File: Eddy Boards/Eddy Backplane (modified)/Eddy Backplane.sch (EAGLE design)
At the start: 88 parts, among them J1 USB_MINI-B_SMT, P1 39-30-02_S, P2 RB1-125BAG1A, P3 39-30-04_S, Q1 310mA/60V/1.6Ω, Q2 310mA/60V/1.6Ω, Q3 310mA/60V/1.6Ω, Q4 310mA/60V/1.6Ω, Q5 310mA/60V/1.6Ω, Q6 310mA/60V/1.6Ω, Q7 310mA/60V/1.6Ω, Q8 310mA/60V/1.6Ω, U1 W5500, U2 STM32F405RGT6, Y2 12MHz, Y3 32.768kHz

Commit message: Routing began on Eddy backplane. New size
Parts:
- removed 16MHZ, 32.768KHZ: (no value), SparkFun-Clocks:CRYSTALPTH-HC49US
- removed C10, C11, C12, C9: (no value), rcl:C-EUC0603
- removed C3, C8: 2.2 uF, rcl:C-EUC0603
- removed U$4: STM32F405RGT6, SparkFun-IC-Microcontroller:STM32F405RG
- added C25, C26, C27, C7: (no value), rcl:C-EUC0603
- added R2, R3, R5, R6: (no value), rcl:R-US_R0603
- renumbered R24 to R1
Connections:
- removed net N$1: C3.1, U$4.VCAP1
- removed net N$2: C8.1, U$4.VCAP2
- removed net N$3: 32.768KHZ.1, C11.1, U$4.PC14
- removed net N$5: 16MHZ.1, C9.1, U$4.PH0
- removed net N$6: 32.768KHZ.2, C12.1, U$4.PC15
- removed net N$7: 16MHZ.2, C10.1, U$4.PH1
- new net N$22: C25.2, R5.2, R6.2
- new net N$23: P2.TD+, R3.2, U1.TXP
- new net N$24: P2.TD-, R2.2, U1.TXN
- new net N$25: C26.2, P2.RD+
- new net N$26: C26.1, R5.1, U1.RXP
- new net N$27: C27.2, R6.1, U1.RXN
- new net N$28: C27.1, P2.RD-
- net +3V3: now also C1.1, C2.1, C4.1, C5.1, C6.1, C7.1, P2.CT, Q1.G, Q2.G, Q3.G, Q4.G, Q5.G, Q6.G, Q7.G, Q8.G, R1.2, R2.1, R23.2, R25.1, R28.1, R3.1, R31.1, R33.1, R35.1, R37.1, R39.1, R41.1
- net 3.3V: no longer C1.1, C2.1, C4.1, C5.1, C6.1, Q1.G, Q2.G, Q3.G, Q4.G, Q5.G, Q6.G, Q7.G, Q8.G, R25.1, R28.1, R31.1, R33.1, R35.1, R37.1, R39.1, R41.1, U$4.VDD1, U$4.VDD2, U$4.VDD3, U$4.VDD4, U$4.VDDA
- net GND: now also C25.1, C7.2; no longer C10.2, C11.2, C12.2, C3.2, C8.2, C9.2, P2.L2, P2.L4, U$4.VSS1, U$4.VSS2, U$4.VSSA
- net KILL_SWITCH: now also SWITCH_CONNECTOR-4.P; no longer SWITCH_CONNECTOR-2.P
- net N$11: now also P2.L4; no longer R1.2
- net N$12: now also P2.L2; no longer R23.2
- net SWITCH_2: now also SWITCH_CONNECTOR-2.P; no longer SWITCH_CONNECTOR-4.P
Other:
- note removed: "Ask Gus about this connection scheme for clarification"

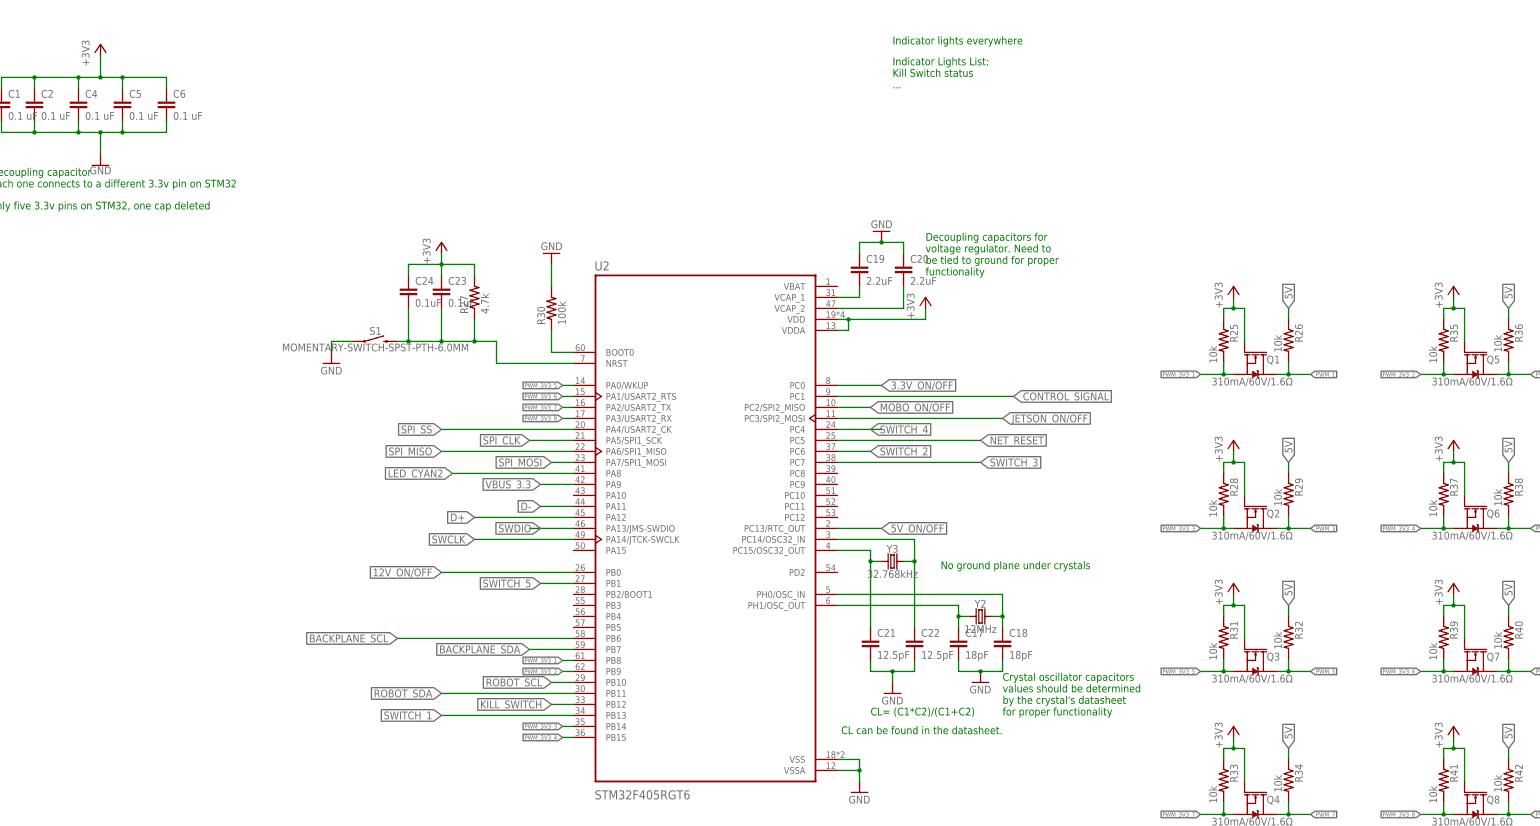
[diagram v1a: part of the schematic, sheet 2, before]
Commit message: further routing done on Copro/backplane
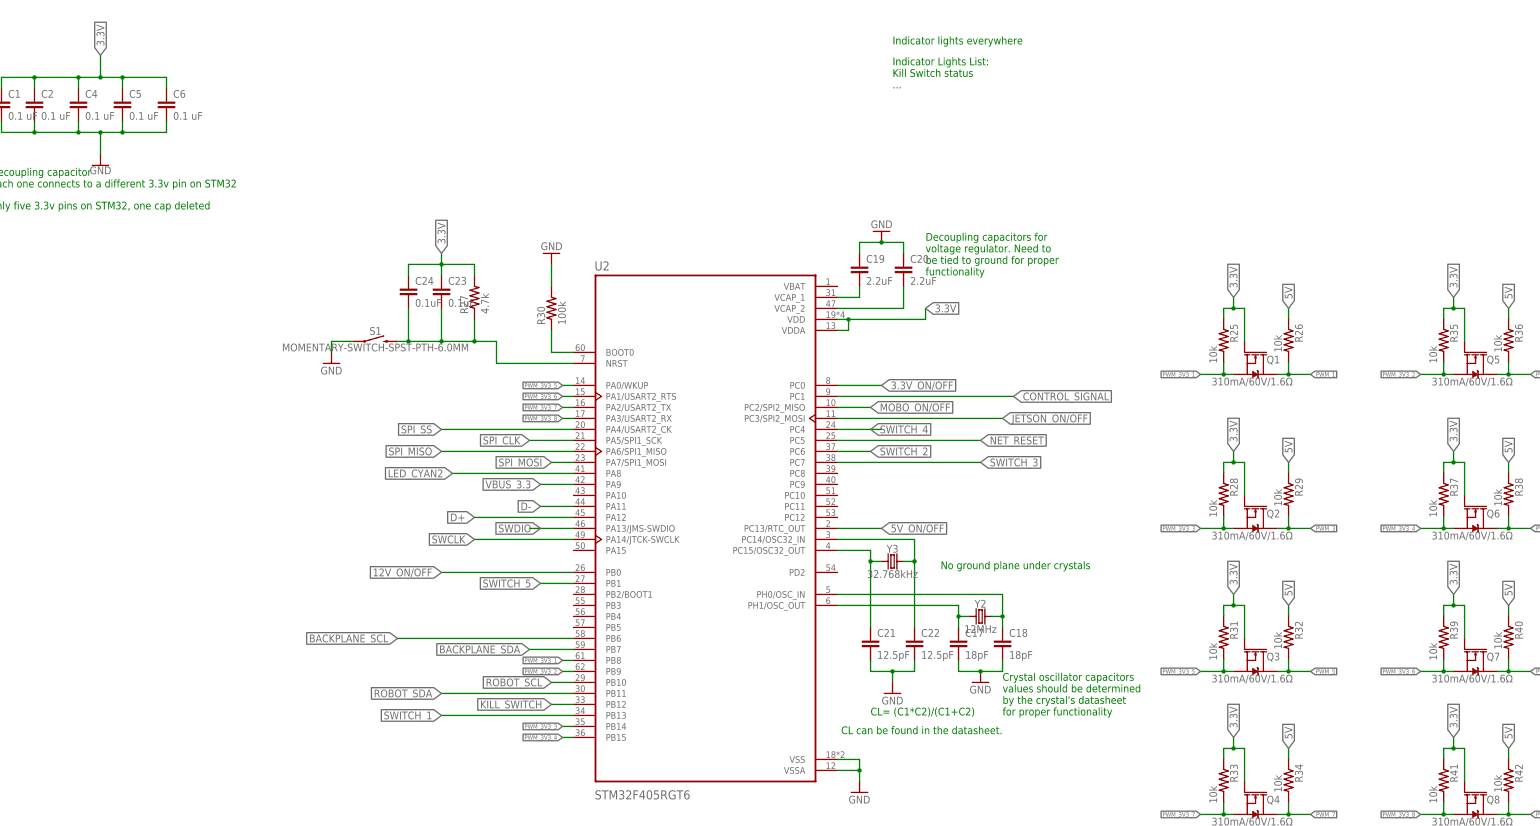
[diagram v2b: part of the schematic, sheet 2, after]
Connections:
- removed net +3V3: C1.1, C2.1, C23.1, C24.1, C4.1, C5.1, C6.1, C7.1, P2.CT, Q1.G, Q2.G, Q3.G, Q4.G, Q5.G, Q6.G, Q7.G, Q8.G, R1.2, R2.1, R23.2, R25.1, R27.2, R28.1, R3.1, R31.1, R33.1, R35.1, R37.1, R39.1, R41.1, SWDIO/SWDCLK/RESET.1, SWDIO/SWDCLK/RESET.2, U1.AVDD, U1.VDD, U2.VDD, U2.VDDA
- net 3.3V: now also C1.1, C2.1, C23.1, C24.1, C4.1, C5.1, C6.1, C7.1, P2.CT, Q1.G, Q2.G, Q3.G, Q4.G, Q5.G, Q6.G, Q7.G, Q8.G, R1.2, R2.1, R23.2, R25.1, R27.2, R28.1, R3.1, R31.1, R33.1, R35.1, R37.1, R39.1, R41.1, SWDIO/SWDCLK/RESET.1, SWDIO/SWDCLK/RESET.2, U1.AVDD, U1.VDD, U2.VDD, U2.VDDA
